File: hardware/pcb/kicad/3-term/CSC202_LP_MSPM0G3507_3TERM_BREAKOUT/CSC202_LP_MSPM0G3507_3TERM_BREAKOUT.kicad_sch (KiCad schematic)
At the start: 6 parts, among them J1 J_IN1/J_IN3, J2 J_IN4/J_IN2, J3 J_OUT1, J4 J_OUT3, J5 J_OUT4, J6 J_OUT2

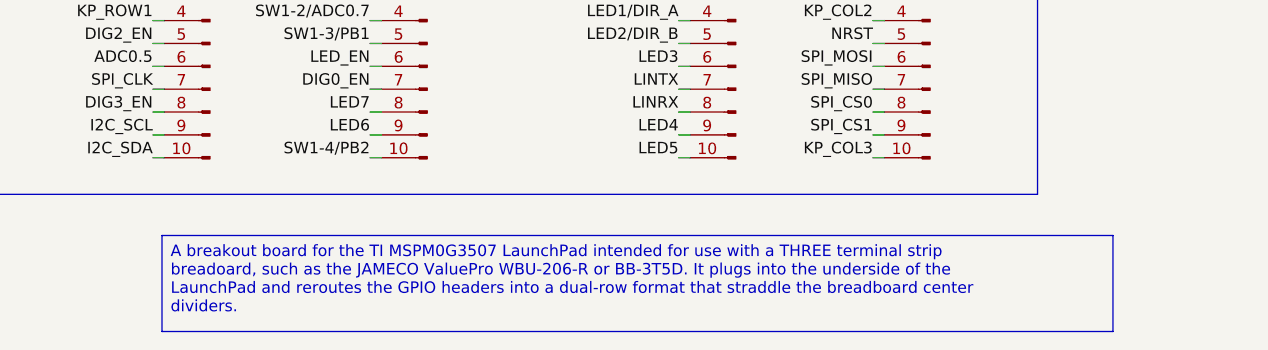
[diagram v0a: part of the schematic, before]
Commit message: implemented kibot and mkdocs
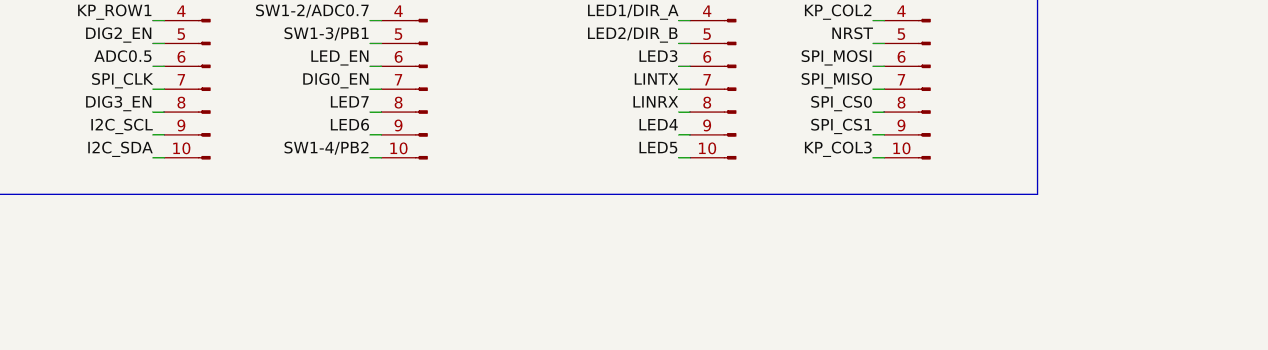
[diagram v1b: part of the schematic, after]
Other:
- company: MCC -> Eli Bell
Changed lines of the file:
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@@
 	(title_block
 		(title "CSC_202_LP_MSPM0G3507_3TERM_BREAKOUT")
-		(company "MCC")
+		(date "2026-01-15")
+		(rev "A")
+		(company "Eli Bell")
+		(comment 1 "format that straddle the breadboard center dividers.")
+		(comment 2 "into the underside of the LaunchPad and reroutes the GPIO headers into a dual-row ")
+		(comment 3 "terminal strip breadoard, such as the JAMECO ValuePro WBU-206-R or BB-3T5D. It plugs ")
+		(comment 4 "A breakout board for the TI MSPM0G3507 LaunchPad intended for use with a THREE")
 	)
 	(rectangle
@@
 		)
 	)
-	(text_box "A breakout board for the TI MSPM0G3507 LaunchPad intended for use with a THREE terminal strip breadoard, such as the JAMECO ValuePro WBU-206-R or BB-3T5D. It plugs into the underside of the LaunchPad and reroutes the GPIO headers into a dual-row format that straddle the breadboard center dividers."
-		(exclude_from_sim no)
-		(at 91.186 105.156 0)
-		(size 105.664 10.668)
-		(margins 0.9525 0.9525 0.9525 0.9525)
-		(stroke
-			(width 0)
-			(type solid)
-		)
-		(fill
-			(type none)
-		)
-		(effects
-			(font
-				(size 1.27 1.27)
-			)
-			(justify left top)
-		)
-	)
